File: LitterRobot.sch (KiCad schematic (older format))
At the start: 4 parts, among them J1 DF11C-4DP-2V(57), J2 DF11C-6DP-2V(57), J3 DF11C-8DP-2V(57), J4 DF11C-6DP-2V(57)

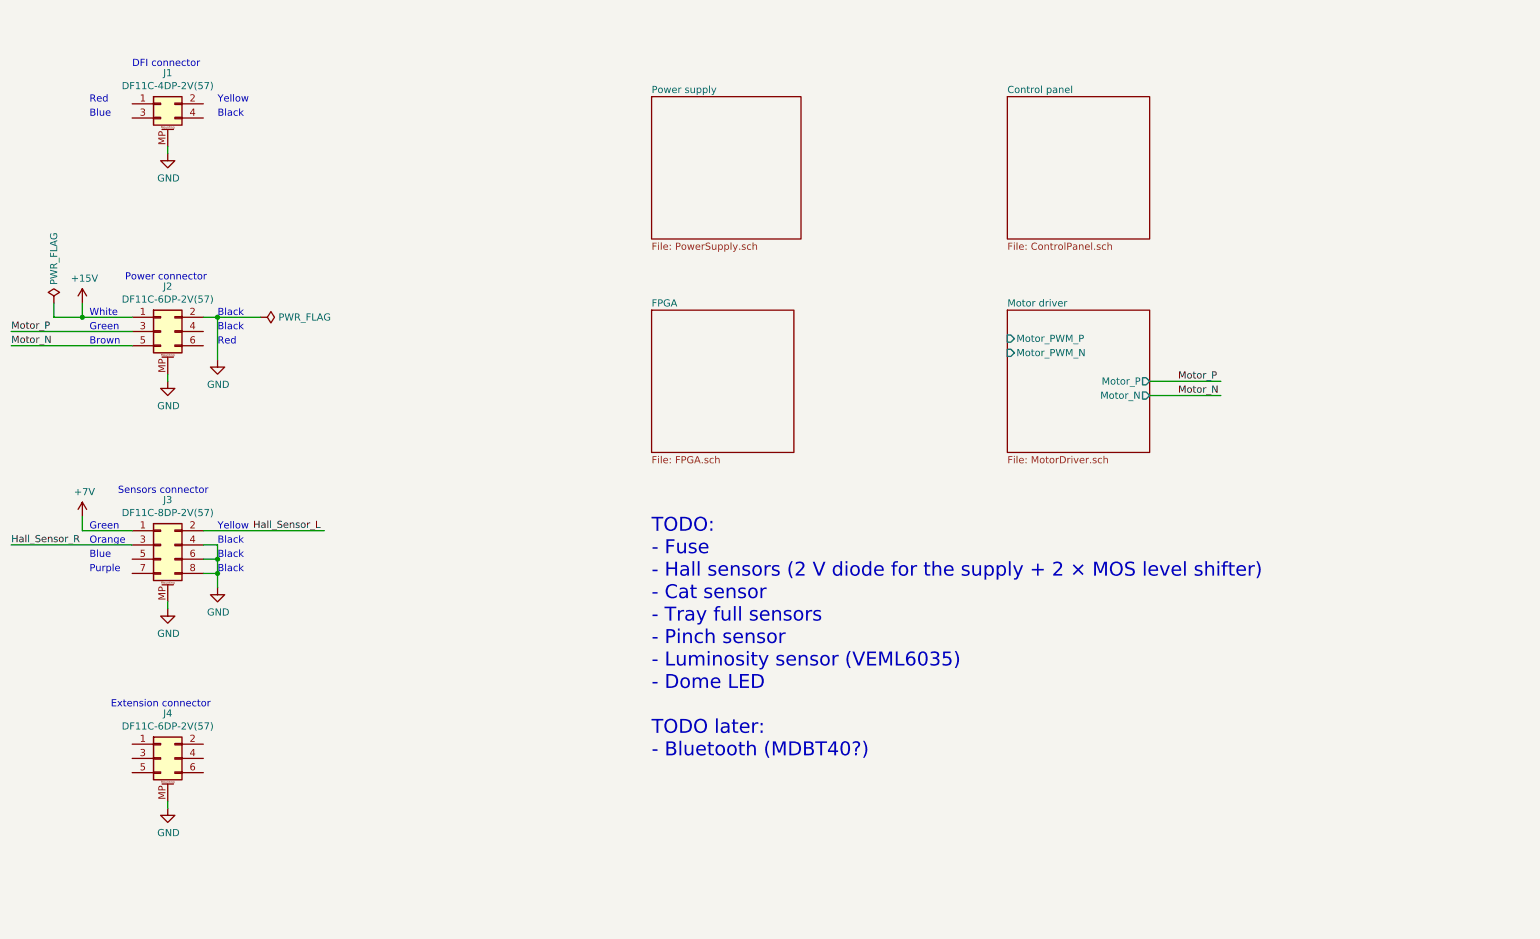
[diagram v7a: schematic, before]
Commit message: Add fuse and more inter-page signals
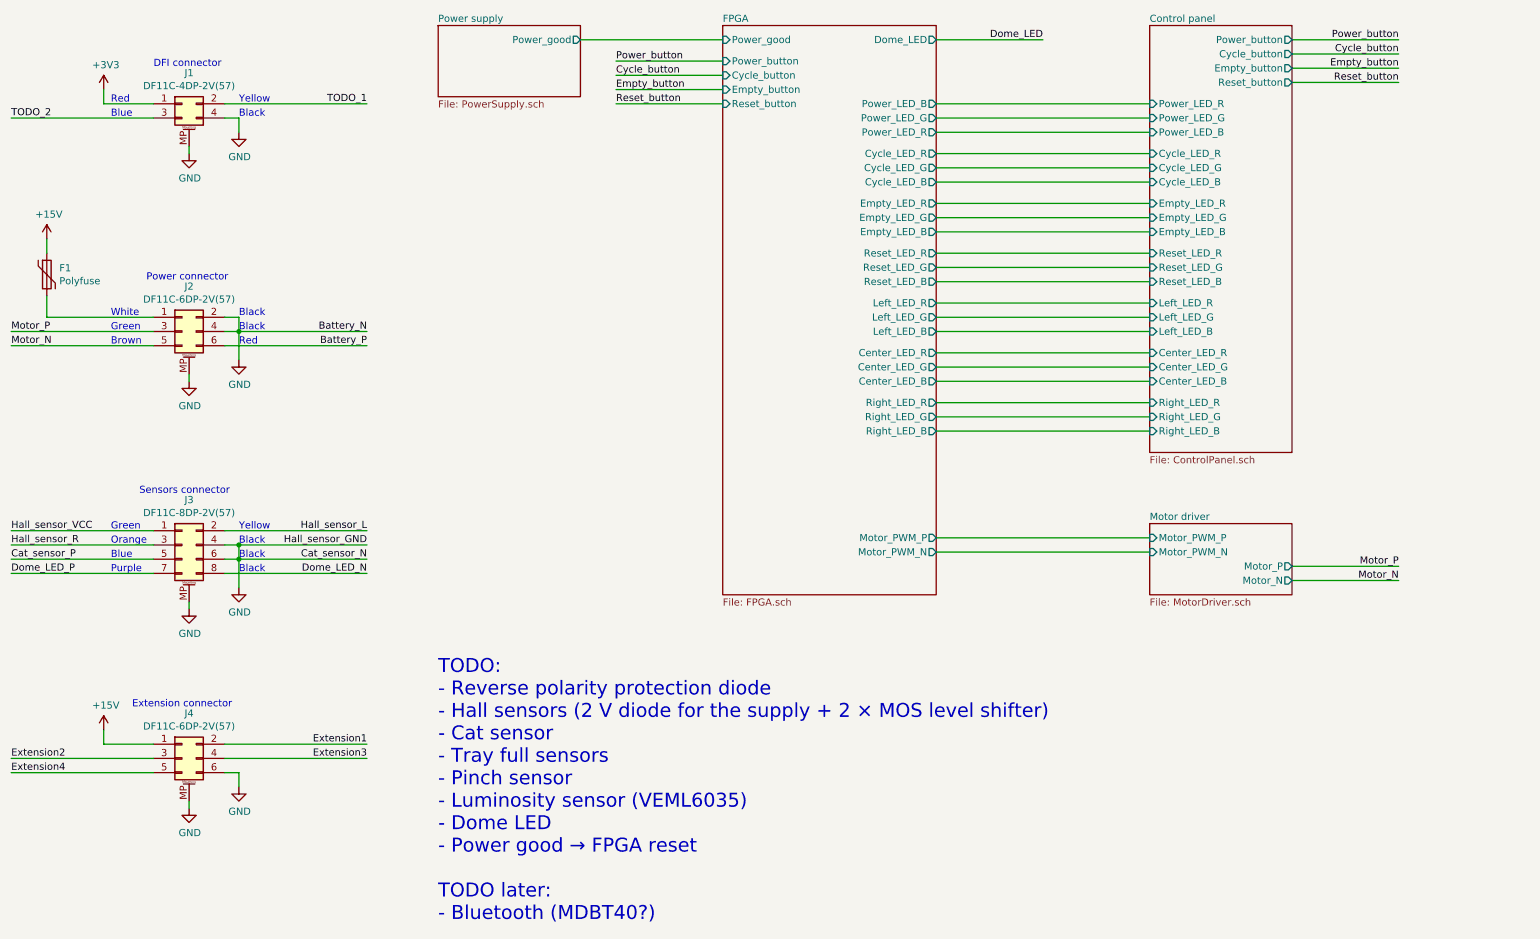
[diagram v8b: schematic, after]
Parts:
- added F1: Polyfuse, LitterRobot:Bel_Fuse_0ZCG, symbol Device:Polyfuse
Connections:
- net labels added: +3V3, Battery_N, Battery_P, Cat_sensor_N, Cat_sensor_P, Cycle_button, Dome_LED, Dome_LED_N, Dome_LED_P, Empty_button, Extension1, Extension2, Extension3, Extension4, Hall_sensor_GND, Hall_sensor_L, Hall_sensor_R, Hall_sensor_VCC, Power_button, Reset_button, TODO_1, TODO_2
- net labels removed: +7V, Hall_Sensor_L, Hall_Sensor_R
- wire segments 25 -> 76
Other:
- note added: "TODO:\n- Reverse polarity protection diode\n- Hall sensors (2 V diode for the supply + 2 × MOS level shifter)\n- Cat sensor\n- Tray full sensors\n- Pinch sensor\n- Luminosity sensor (VEML6035)\n- Dome LED\n- Power good → FPGA reset\n\nTODO later:\n- Bluetooth (MDBT40?)"
- note removed: "TODO:\n- Fuse\n- Hall sensors (2 V diode for the supply + 2 × MOS level shifter)\n- Cat sensor\n- Tray full sensors\n- Pinch sensor\n- Luminosity sensor (VEML6035)\n- Dome LED\n\nTODO later:\n- Bluetooth (MDBT40?)"
- moved on the sheet: J1, J2, J3, J4
